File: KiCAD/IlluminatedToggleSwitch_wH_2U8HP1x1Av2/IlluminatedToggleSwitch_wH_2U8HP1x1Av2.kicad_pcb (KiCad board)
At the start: 2 copper layers, 40.3 x 84 mm, 8 parts, among them SW1 SW_Covered_SPST_w/LED_Panel_M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, SW2 SW_SPST_M6_MOUNT

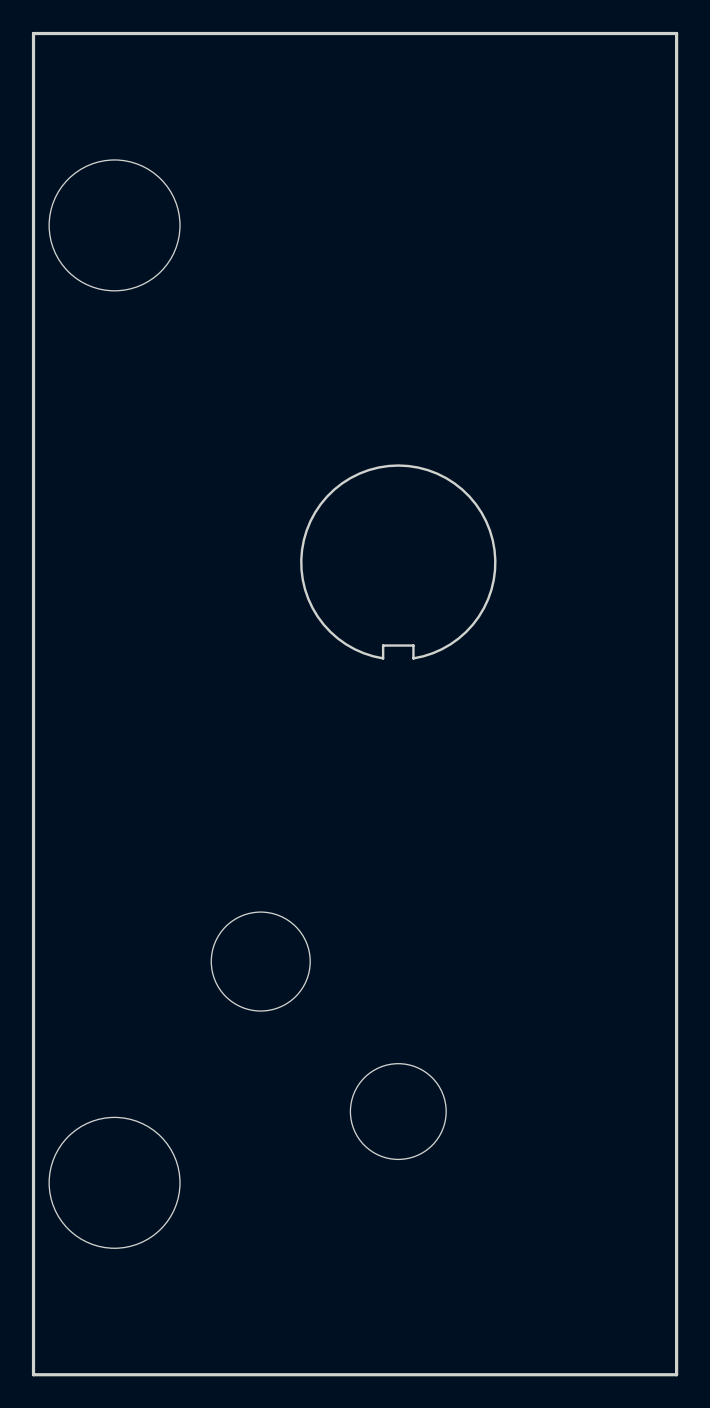
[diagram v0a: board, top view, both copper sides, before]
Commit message: updated all modules to use plated through-holes wherever possible
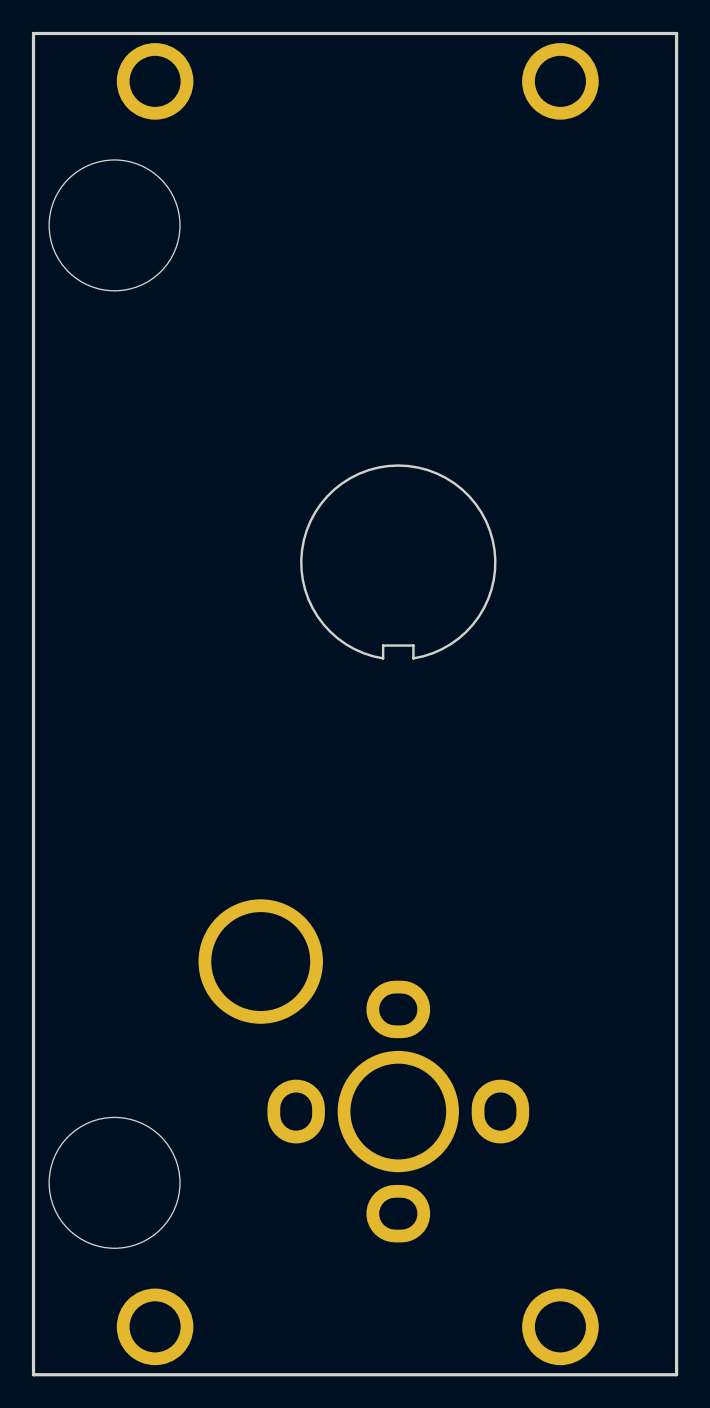
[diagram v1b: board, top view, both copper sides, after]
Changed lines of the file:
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@@
 			)
 		)
-		(pad "" np_thru_hole oval
+		(pad "" thru_hole circle
 			(at 0 0)
-			(size 4.34 3.2)
-			(drill oval 4.34 3.2)
-			(layers "*.Cu" "*.Mask")
+			(size 4.8 4.8)
+			(drill 3.2)
+			(layers "*.Cu" "*.Mask")
+			(remove_unused_layers no)
 		)
 		(embedded_fonts no)
@@
 			)
 		)
-		(pad "" np_thru_hole oval
+		(pad "" thru_hole circle
 			(at 0 0)
-			(size 4.34 3.2)
-			(drill oval 4.34 3.2)
-			(layers "*.Cu" "*.Mask")
+			(size 4.8 4.8)
+			(drill 3.2)
+			(layers "*.Cu" "*.Mask")
+			(remove_unused_layers no)
 		)
 		(embedded_fonts no)
@@
 			)
 		)
-		(pad "" np_thru_hole oval
+		(pad "" thru_hole oval
 			(at -6.4 0)
-			(size 2 2.4)
+			(size 3.6 4)
 			(drill oval 2 2.4)
 			(layers "*.Cu" "*.Mask")
-		)
-		(pad "" np_thru_hole oval
+			(remove_unused_layers no)
+		)
+		(pad "" thru_hole oval
 			(at 0 -6.4)
-			(size 2.4 2)
+			(size 4 3.6)
 			(drill oval 2.4 2)
 			(layers "*.Cu" "*.Mask")
-		)
-		(pad "" np_thru_hole circle
+			(remove_unused_layers no)
+		)
+		(pad "" thru_hole circle
 			(at 0 0)
-			(size 6 6)
+			(size 7.6 7.6)
 			(drill 6)
 			(layers "*.Cu" "*.Mask")
-		)
-		(pad "" np_thru_hole oval
+			(remove_unused_layers no)
+		)
+		(pad "" thru_hole oval
 			(at 0 6.4)
-			(size 2.4 2)
+			(size 4 3.6)
 			(drill oval 2.4 2)
 			(layers "*.Cu" "*.Mask")
-		)
-		(pad "" np_thru_hole oval
+			(remove_unused_layers no)
+		)
+		(pad "" thru_hole oval
 			(at 6.4 0)
-			(size 2 2.4)
+			(size 3.6 4)
 			(drill oval 2 2.4)
 			(layers "*.Cu" "*.Mask")
+			(remove_unused_layers no)
 		)
 		(embedded_fonts no)
@@
 			)
 		)
-		(pad "" np_thru_hole oval
+		(pad "" thru_hole circle
 			(at 0 0)
-			(size 4.34 3.2)
-			(drill oval 4.34 3.2)
-			(layers "*.Cu" "*.Mask")
+			(size 4.8 4.8)
+			(drill 3.2)
+			(layers "*.Cu" "*.Mask")
+			(remove_unused_layers no)
 		)
 		(embedded_fonts no)
@@
 			)
 		)
-		(pad "" np_thru_hole circle
+		(pad "" thru_hole circle
 			(at 0 0)
-			(size 6.2 6.2)
+			(size 7.8 7.8)
 			(drill 6.2)
 			(layers "*.Cu" "*.Mask")
+			(remove_unused_layers no)
 		)
 		(embedded_fonts no)
@@
 			)
 		)
-		(pad "" np_thru_hole oval
+		(pad "" thru_hole circle
 			(at 0 0)
-			(size 4.34 3.2)
-			(drill oval 4.34 3.2)
-			(layers "*.Cu" "*.Mask")
+			(size 4.8 4.8)
+			(drill 3.2)
+			(layers "*.Cu" "*.Mask")
+			(remove_unused_layers no)
 		)
 		(embedded_fonts no)
